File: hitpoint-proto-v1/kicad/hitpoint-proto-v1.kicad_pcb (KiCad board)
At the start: 2 copper layers, 45 x 45 mm, 21 parts, among them J1 Conn_01x05_Male, J2 Conn_01x06_Female, J3 Conn_01x06_Female, U1 STM32G030Fx, U2 IRM-H6XXT

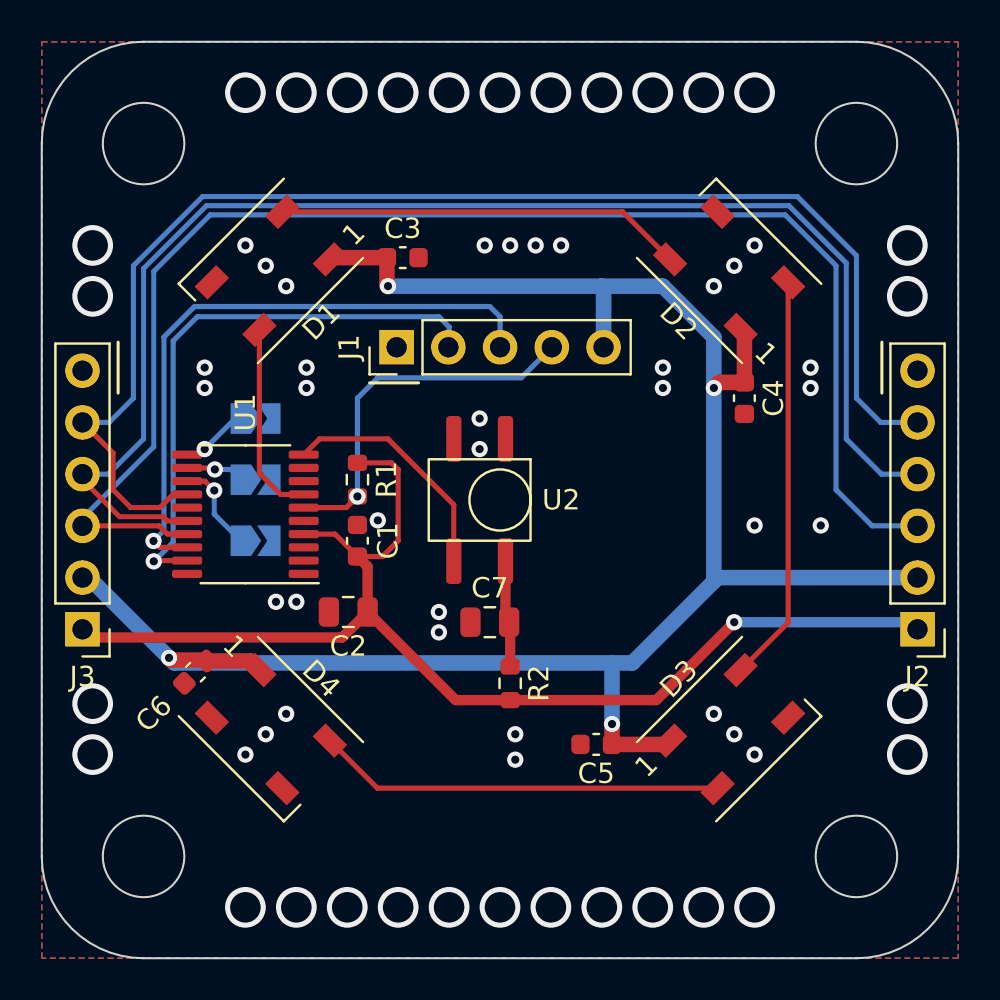
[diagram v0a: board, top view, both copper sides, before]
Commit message: Added some more ground vias
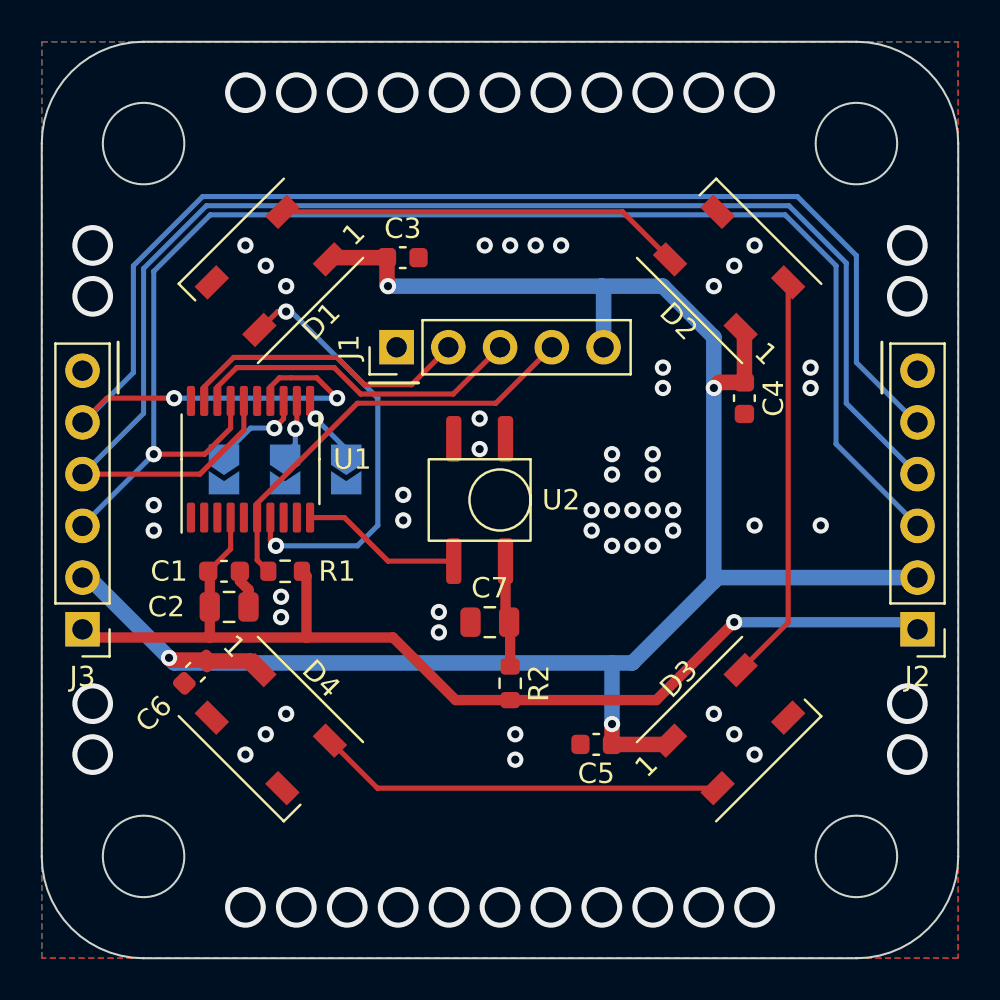
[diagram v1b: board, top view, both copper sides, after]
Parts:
- moved C1 6.72 mm to (124.0, 91.0), turned to 0 degrees
- moved C2 5.86 mm to (124.2, 92.8), turned to 0 degrees
- moved R1 5.73 mm to (127.0, 91.0), turned to 180 degrees
- moved MCFG0 5.10 mm to (129.9, 86.0), turned to -90 degrees
- moved MCFG2 3.83 mm to (124.0, 86.0), turned to -90 degrees
- moved U1 2.71 mm to (125.2, 85.5), turned to 90 degrees
- moved MCFG1 1.53 mm to (127.0, 86.0), turned to -90 degrees
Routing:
- net SWDIO: track 30.8 -> 16.5 mm, vias 1 -> 0
- net SWCLK: track 28.1 -> 14.7 mm, vias 1 -> 0
- net LED_DIN: track 9.64 -> 21.1 mm, vias 0 -> 2
- net I2C_IRQ: track 66.3 -> 73.9 mm, vias 0 -> 2
- net +3V3: track 59.2 -> 53.9 mm
- net IR_DATA: track 11.8 -> 7.94 mm
- net NRST: track 18.3 -> 21.2 mm, vias 1 -> 0
- net I2C_SCL: track 68.1 -> 70.6 mm
- net GND: track 0.00 -> 1.93 mm, vias 65 -> 78
- net I2C_SDA: track 70.7 -> 69.7 mm, vias 0 -> 1
